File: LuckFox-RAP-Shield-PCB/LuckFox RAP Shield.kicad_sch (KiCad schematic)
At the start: 4 parts, among them J1 LuckFox_Pico_Mini_Connector, J2 External_5V_Input_from_Buck_M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, U2 W5500_Ethernet_Module_DNP_on_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

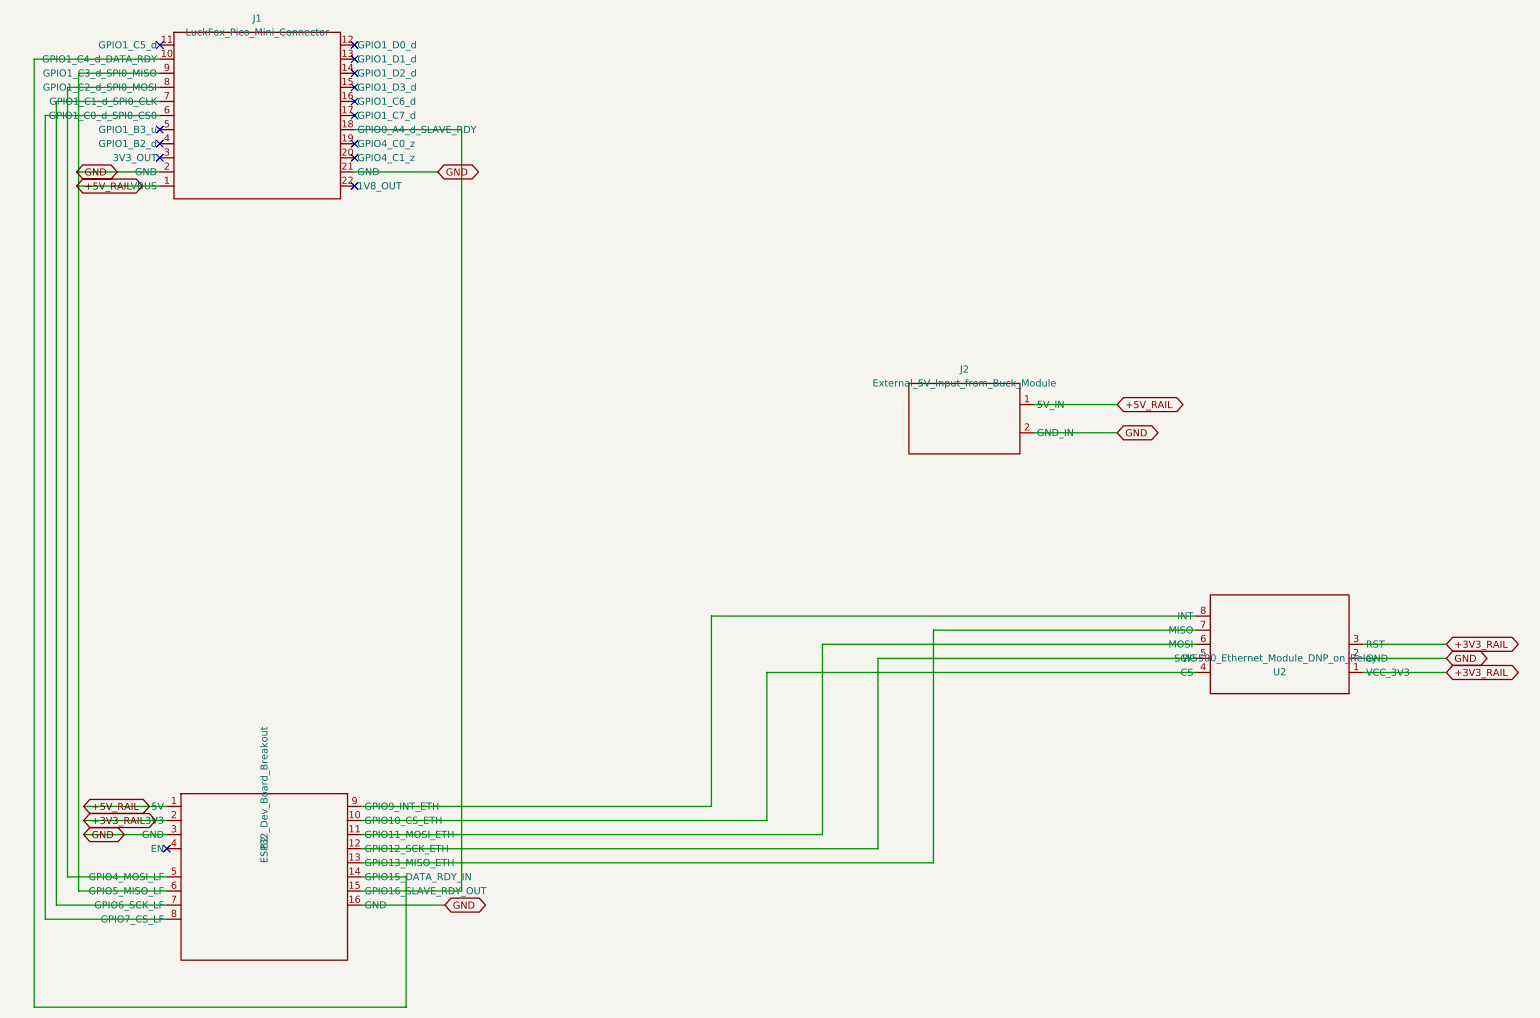
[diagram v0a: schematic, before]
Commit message: Fix double-extension bug: pin (at x y) is already the connection point
The real bug (unrelated to mirror or rotation direction): a KiCad pin's
(at lx ly angle) coordinate already IS the electrical connection tip --
length only draws the visual stub line back toward the body, it does not
push the connection point further out. The previous rewrite was adding
length*(cos,sin) on top of the already-correct tip, overshooting every
pin by 2.54mm and leaving every wire touching empty space. Removed the
length extension; wires now terminate exactly at each pin's (at x y).
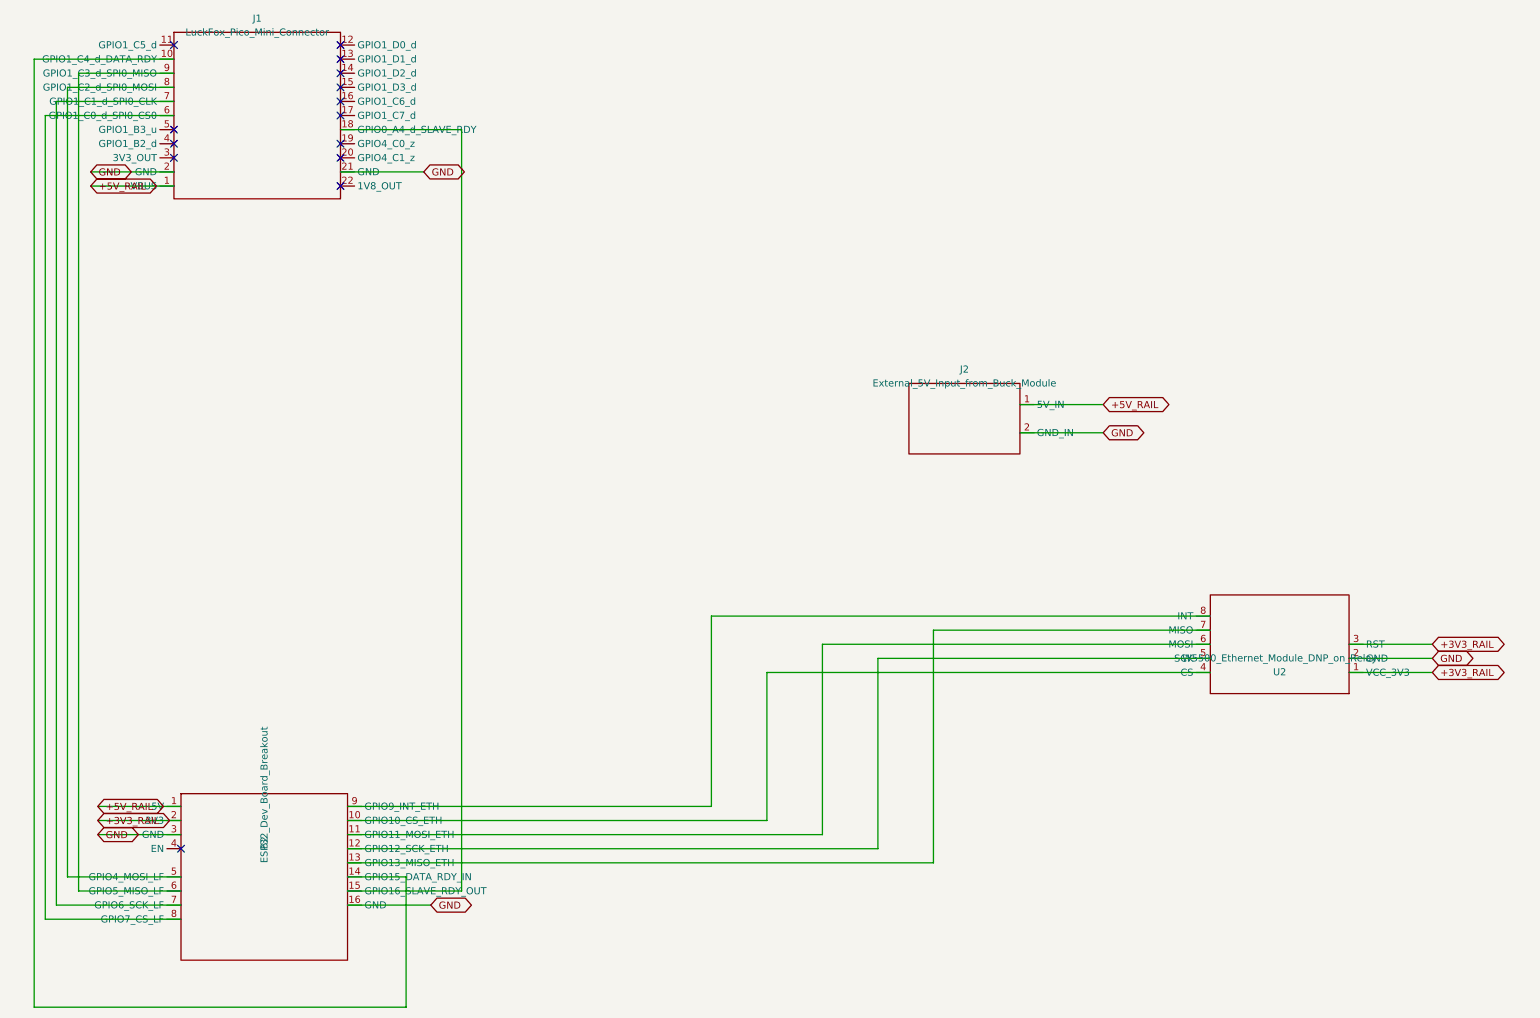
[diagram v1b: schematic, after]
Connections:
- net +3V3_RAIL: now also B2.2 (3V3), U2.1 (VCC_3V3), U2.3 (RST)
- net +5V_RAIL: now also B2.1 (5V), J1.1 (VBUS), J2.1 (5V_IN)
- net GND: now also B2.16 (GND), B2.3 (GND), J1.2 (GND), J1.21 (GND), J2.2 (GND_IN), U2.2 (GND)
- net at B2.10 (GPIO10_CS_ETH): now also U2.4 (CS)
- net at B2.11 (GPIO11_MOSI_ETH): now also U2.6 (MOSI)
- net at B2.12 (GPIO12_SCK_ETH): now also U2.5 (SCK)
- net at B2.13 (GPIO13_MISO_ETH): now also U2.7 (MISO)
- net at B2.14 (GPIO15_DATA_RDY_IN): now also J1.10 (GPIO1_C4_d_DATA_RDY)
- net at B2.15 (GPIO16_SLAVE_RDY_OUT): now also J1.18 (GPIO0_A4_d_SLAVE_RDY)
- net at B2.5 (GPIO4_MOSI_LF): now also J1.8 (GPIO1_C2_d_SPI0_MOSI)
- net at B2.6 (GPIO5_MISO_LF): now also J1.9 (GPIO1_C3_d_SPI0_MISO)
- net at B2.7 (GPIO6_SCK_LF): now also J1.7 (GPIO1_C1_d_SPI0_CLK)
- net at B2.8 (GPIO7_CS_LF): now also J1.6 (GPIO1_C0_d_SPI0_CS0)
- net at B2.9 (GPIO9_INT_ETH): now also U2.8 (INT)

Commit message: Add PWR_FLAG symbols to +5V_RAIL, +3V3_RAIL, GND to silence ERC
Those 3 nets are only fed by unmodeled external sources (buck module via
J2, and implicit board GND), so ERC's power_pin_not_driven check has no
power_out pin to see. A standard power:PWR_FLAG symbol on each net tells
ERC the net is intentionally externally driven.
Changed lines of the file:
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@@
+		)
+	)
+	(symbol
+		(lib_id "power:PWR_FLAG")
+		(at 29.45 163.83 0)
+		(unit 1)
+		(exclude_from_sim no)
+		(in_bom yes)
+		(on_board yes)
+		(dnp no)
+		(fields_autoplaced yes)
+		(property "Reference" "#FLG01"
+			(at 29.45 161.29 0)
+			(show_name no)
+			(do_not_autoplace no)
+			(effects
+				(font
+					(size 1.27 1.27)
+				)
+				(hide yes)
+			)
+		)
+		(property "Value" "PWR_FLAG"
+			(at 29.45 160.02 0)
+			(show_name no)
+			(do_not_autoplace no)
+			(effects
+				(font
+					(size 1.27 1.27)
+				)
+			)
+		)
+		(property "Footprint" ""
+			(at 29.45 163.83 0)
+			(show_name no)
+			(do_not_autoplace no)
+			(effects
+				(font
+					(size 1.27 1.27)
+				)
+				(hide yes)
+			)
+		)
+		(property "Datasheet" ""
+			(at 29.45 163.83 0)
+			(show_name no)
+			(do_not_autoplace no)
+			(effects
+				(font
+					(size 1.27 1.27)
+				)
+				(hide yes)
+			)
+		)
+		(property "Description" ""
+			(at 29.45 163.83 0)
+			(show_name no)
+			(do_not_autoplace no)
+			(effects
+				(font
+					(size 1.27 1.27)
+				)
+				(hide yes)
+			)
+		)
+		(pin "1"
+		)
+		(instances
+			(project "LuckFox RAP Shield"
+				(path "/e63e39d7-6ac0-4ffd-8aa3-1841a4541b55"
+					(reference "#FLG01")
+					(unit 1)
+				)
+			)
+		)
+	)
+	(symbol
+		(lib_id "power:PWR_FLAG")
+		(at 29.45 166.37 0)
+		(unit 1)
+		(exclude_from_sim no)
+		(in_bom yes)
+		(on_board yes)
+		(dnp no)
+		(fields_autoplaced yes)
+		(property "Reference" "#FLG02"
+			(at 29.45 163.83 0)
+			(show_name no)
+			(do_not_autoplace no)
+			(effects
+				(font
+					(size 1.27 1.27)
+				)
+				(hide yes)
+			)
+		)
+		(property "Value" "PWR_FLAG"
+			(at 29.45 162.56 0)
+			(show_name no)
+			(do_not_autoplace no)
+			(effects
+				(font
+					(size 1.27 1.27)
+				)
+			)
+		)
+		(property "Footprint" ""
+			(at 29.45 166.37 0)
+			(show_name no)
+			(do_not_autoplace no)
+			(effects
+				(font
+					(size 1.27 1.27)
+				)
+				(hide yes)
+			)
+		)
+		(property "Datasheet" ""
+			(at 29.45 166.37 0)
+			(show_name no)
+			(do_not_autoplace no)
+			(effects
+				(font
+					(size 1.27 1.27)
+				)
+				(hide yes)
+			)
+		)
+		(property "Description" ""
+			(at 29.45 166.37 0)
+			(show_name no)
+			(do_not_autoplace no)
+			(effects
+				(font
+					(size 1.27 1.27)
+				)
+				(hide yes)
+			)
+		)
+		(pin "1"
+		)
+		(instances
+			(project "LuckFox RAP Shield"
+				(path "/e63e39d7-6ac0-4ffd-8aa3-1841a4541b55"
+					(reference "#FLG02")
+					(unit 1)
+				)
+			)
+		)
+	)
+	(symbol
+		(lib_id "power:PWR_FLAG")
+		(at 29.45 168.91 0)
+		(unit 1)
+		(exclude_from_sim no)
+		(in_bom yes)
+		(on_board yes)
+		(dnp no)
+		(fields_autoplaced yes)
+		(property "Reference" "#FLG03"
+			(at 29.45 166.37 0)
+			(show_name no)
+			(do_not_autoplace no)
+			(effects
+				(font
+					(size 1.27 1.27)
+				)
+				(hide yes)
+			)
+		)
+		(property "Value" "PWR_FLAG"
+			(at 29.45 165.10 0)
+			(show_name no)
+			(do_not_autoplace no)
+			(effects
+				(font
+					(size 1.27 1.27)
+				)
+			)
+		)
+		(property "Footprint" ""
+			(at 29.45 168.91 0)
+			(show_name no)
+			(do_not_autoplace no)
+			(effects
+				(font
+					(size 1.27 1.27)
+				)
+				(hide yes)
+			)
+		)
+		(property "Datasheet" ""
+			(at 29.45 168.91 0)
+			(show_name no)
+			(do_not_autoplace no)
+			(effects
+				(font
+					(size 1.27 1.27)
+				)
+				(hide yes)
+			)
+		)
+		(property "Description" ""
+			(at 29.45 168.91 0)
+			(show_name no)
+			(do_not_autoplace no)
+			(effects
+				(font
+					(size 1.27 1.27)
+				)
+				(hide yes)
+			)
+		)
+		(pin "1"
+		)
+		(instances
+			(project "LuckFox RAP Shield"
+				(path "/e63e39d7-6ac0-4ffd-8aa3-1841a4541b55"
+					(reference "#FLG03")
+					(unit 1)
+				)
+			)
 		)
 	)
